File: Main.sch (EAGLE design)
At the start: 27 parts, among them IC2 74AHC1G125DBV, IC3 74AHC1G125DBV, M1 HX1, X1 BU-SMA-V

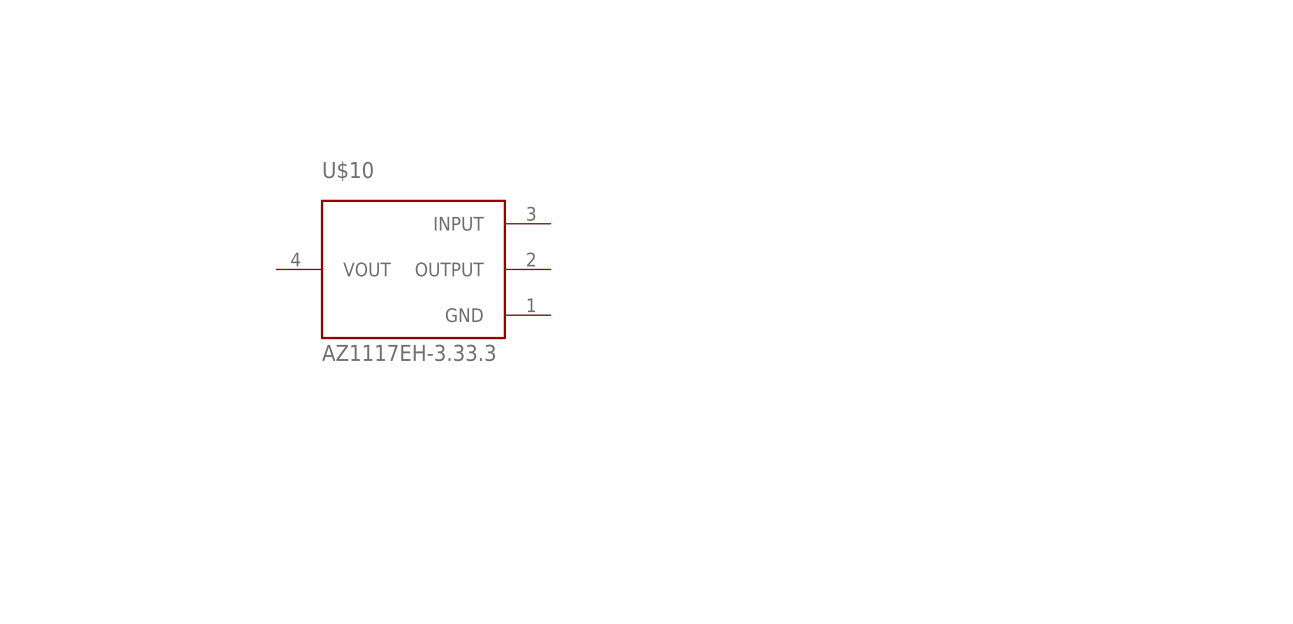
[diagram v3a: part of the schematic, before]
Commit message: Both Voltage Regs added and made
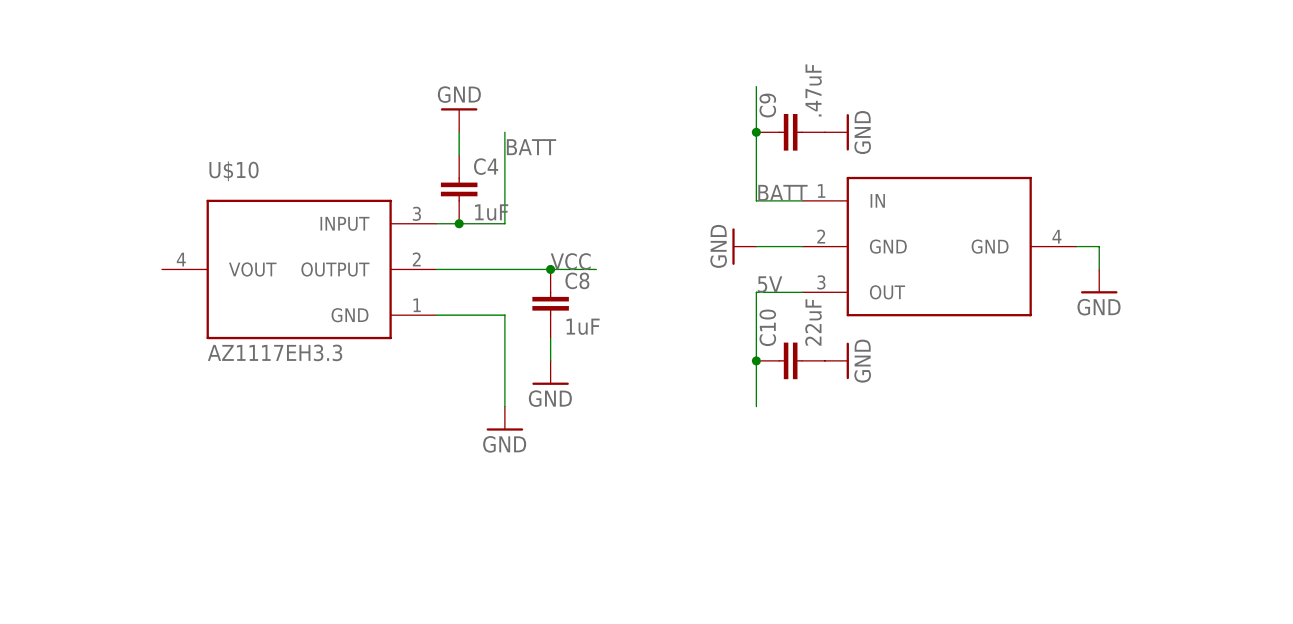
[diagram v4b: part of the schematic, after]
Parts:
- added C10: 22uF, SparkFun:CAP0603-CAP
- added C4, C8: 1uF, SparkFun:CAP0603-CAP
- added C9: .47uF, SparkFun:CAP0603-CAP
- added U$11: LM2940-5, Physoon:LM2940-5
- U$10: value AZ1117EH-3.33.3 -> AZ1117EH3.3; device Physoon:AZ1117EH-3.33.3 -> Physoon:AZ1117EH3.3
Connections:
- net 5V: now also C10.1, U$11.OUT
- net BATT: now also C4.2, C9.1, U$10.INPUT, U$11.IN
- net GND: now also C10.2, C4.1, C8.2, C9.2, U$10.GND, U$11.GND, U$11.GND@2
- net VCC: now also C8.1, U$10.OUTPUT
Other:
- moved on the sheet: U$10
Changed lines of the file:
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@@
 <setting verticaltext="up"/>
 </settings>
-<grid distance="0.1" unitdist="inch" unit="inch" style="lines" multiple="1" display="no" altdistance="0.01" altunitdist="inch" altunit="inch"/>
+<grid distance="0.1" unitdist="inch" unit="inch" style="lines" multiple="1" display="yes" altdistance="0.01" altunitdist="inch" altunit="inch"/>
 <layers>
 <layer number="1" name="Top" color="4" fill="1" visible="no" active="no"/>
@@
 <part name="GND23" library="SparkFun-Aesthetics" deviceset="GND" device=""/>
 <part name="GND24" library="SparkFun-Aesthetics" deviceset="GND" device=""/>
-<part name="U$10" library="Physoon" deviceset="AZ1117EH-3.3" device="3.3"/>
+<part name="U$10" library="Physoon" deviceset="AZ1117EH" device="3.3"/>
+<part name="GND25" library="SparkFun" deviceset="GND" device=""/>
+<part name="C4" library="SparkFun" deviceset="CAP" device="0603-CAP" value="1uF"/>
+<part name="C8" library="SparkFun" deviceset="CAP" device="0603-CAP" value="1uF"/>
+<part name="GND26" library="SparkFun" deviceset="GND" device=""/>
+<part name="GND27" library="SparkFun" deviceset="GND" device=""/>
+<part name="U$11" library="Physoon" deviceset="LM2940" device="-5"/>
+<part name="GND28" library="SparkFun" deviceset="GND" device=""/>
+<part name="GND29" library="SparkFun" deviceset="GND" device=""/>
+<part name="C9" library="SparkFun" deviceset="CAP" device="0603-CAP" value=".47uF"/>
+<part name="C10" library="SparkFun" deviceset="CAP" device="0603-CAP" value="22uF"/>
+<part name="GND30" library="SparkFun" deviceset="GND" device=""/>
+<part name="GND31" library="SparkFun" deviceset="GND" device=""/>
 </parts>
 <sheets>
@@
 <instance part="GND23" gate="1" x="2.54" y="66.04"/>
 <instance part="GND24" gate="1" x="-78.74" y="-29.21" rot="R270"/>
-<instance part="U$10" gate="G$1" x="71.12" y="185.42"/>
+<instance part="U$10" gate="G$1" x="58.42" y="185.42"/>
+<instance part="GND25" gate="1" x="81.28" y="167.64"/>
+<instance part="C4" gate="G$1" x="76.2" y="193.04"/>
+<instance part="C8" gate="G$1" x="86.36" y="180.34"/>
+<instance part="GND26" gate="1" x="86.36" y="172.72"/>
+<instance part="GND27" gate="1" x="76.2" y="203.2" rot="R180"/>
+<instance part="U$11" gate="G$1" x="129.54" y="187.96"/>
+<instance part="GND28" gate="1" x="106.68" y="187.96" rot="R270"/>
+<instance part="GND29" gate="1" x="147.32" y="182.88"/>
+<instance part="C9" gate="G$1" x="114.3" y="200.66" rot="R90"/>
+<instance part="C10" gate="G$1" x="114.3" y="175.26" rot="R90"/>
+<instance part="GND30" gate="1" x="119.38" y="200.66" rot="R90"/>
+<instance part="GND31" gate="1" x="119.38" y="175.26" rot="R90"/>
 </instances>
 <busses>
@@
 <junction x="109.22" y="45.72"/>
 <label x="109.22" y="43.18" size="1.778" layer="95"/>
+</segment>
+<segment>
+<pinref part="U$10" gate="G$1" pin="OUTPUT"/>
+<wire x1="73.66" y1="185.42" x2="86.36" y2="185.42" width="0.1524" layer="91"/>
+<label x="86.36" y="185.42" size="1.778" layer="95"/>
+<pinref part="C8" gate="G$1" pin="1"/>
+<wire x1="86.36" y1="185.42" x2="91.44" y2="185.42" width="0.1524" layer="91"/>
+<junction x="86.36" y="185.42"/>
 </segment>
 </net>
@@
 <wire x1="-71.12" y1="-29.21" x2="-76.2" y2="-29.21" width="0.1524" layer="91"/>
 <pinref part="GND24" gate="1" pin="GND"/>
+</segment>
+<segment>
+<pinref part="U$10" gate="G$1" pin="GND"/>
+<wire x1="73.66" y1="180.34" x2="81.28" y2="180.34" width="0.1524" layer="91"/>
+<wire x1="81.28" y1="180.34" x2="81.28" y2="170.18" width="0.1524" layer="91"/>
+<pinref part="GND25" gate="1" pin="GND"/>
+</segment>
+<segment>
+<pinref part="C8" gate="G$1" pin="2"/>
+<pinref part="GND26" gate="1" pin="GND"/>
+<wire x1="86.36" y1="175.26" x2="86.36" y2="177.8" width="0.1524" layer="91"/>
+</segment>
+<segment>
+<pinref part="C4" gate="G$1" pin="1"/>
+<pinref part="GND27" gate="1" pin="GND"/>
+<wire x1="76.2" y1="200.66" x2="76.2" y2="198.12" width="0.1524" layer="91"/>
+</segment>
+<segment>
+<pinref part="U$11" gate="G$1" pin="GND"/>
+<wire x1="114.3" y1="187.96" x2="109.22" y2="187.96" width="0.1524" layer="91"/>
+<pinref part="GND28" gate="1" pin="GND"/>
+</segment>
+<segment>
+<pinref part="U$11" gate="G$1" pin="GND@2"/>
+<wire x1="144.78" y1="187.96" x2="147.32" y2="187.96" width="0.1524" layer="91"/>
+<wire x1="147.32" y1="187.96" x2="147.32" y2="185.42" width="0.1524" layer="91"/>
+<pinref part="GND29" gate="1" pin="GND"/>
+</segment>
+<segment>
+<pinref part="C9" gate="G$1" pin="2"/>
+<pinref part="GND30" gate="1" pin="GND"/>
+</segment>
+<segment>
+<pinref part="C10" gate="G$1" pin="2"/>
+<pinref part="GND31" gate="1" pin="GND"/>
 </segment>
 </net>
@@
 <label x="-53.34" y="154.94" size="1.778" layer="95"/>
 </segment>
+<segment>
+<pinref part="U$11" gate="G$1" pin="OUT"/>
+<wire x1="114.3" y1="182.88" x2="109.22" y2="182.88" width="0.1524" layer="91"/>
+<wire x1="109.22" y1="182.88" x2="109.22" y2="175.26" width="0.1524" layer="91"/>
+<pinref part="C10" gate="G$1" pin="1"/>
+<wire x1="109.22" y1="175.26" x2="109.22" y2="170.18" width="0.1524" layer="91"/>
+<junction x="109.22" y="175.26"/>
+<label x="109.22" y="182.88" size="1.778" layer="95"/>
+</segment>
 </net>
 <net name="TXD-5V" class="0">
@@
 <label x="-41.91" y="-29.21" size="1.778" layer="95"/>
 </segment>
-</net>
+<segment>
+<pinref part="U$10" gate="G$1" pin="INPUT"/>
+<wire x1="73.66" y1="190.5" x2="76.2" y2="190.5" width="0.1524" layer="91"/>
+<wire x1="76.2" y1="190.5" x2="81.28" y2="190.5" width="0.1524" layer="91"/>
+<wire x1="81.28" y1="190.5" x2="81.28" y2="200.66" width="0.1524" layer="91"/>
+<label x="81.28" y="198.12" size="1.778" layer="95"/>
+<pinref part="C4" gate="G$1" pin="2"/>
+<junction x="76.2" y="190.5"/>
+</segment>
+<segment>
+<pinref part="U$11" gate="G$1" pin="IN"/>
+<wire x1="114.3" y1="193.04" x2="109.22" y2="193.04" width="0.1524" layer="91"/>
+<wire x1="109.22" y1="193.04" x2="109.22" y2="200.66" width="0.1524" layer="91"/>
+<pinref part="C9" gate="G$1" pin="1"/>
+<wire x1="109.22" y1="200.66" x2="109.22" y2="205.74" width="0.1524" layer="91"/>
+<junction x="109.22" y="200.66"/>
+<label x="109.22" y="193.04" size="1.778" layer="95"/>
+</segment>
+</net>

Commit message: More work
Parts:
- added JP4: (no value), SparkFun:M06POLAR
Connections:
- new net RXD: IC1.!!OC0CRXD0PD2, JP4.3
- new net SSC: IC1.PC4/OC1A/#SS, U$1.!CS!
- new net TXD: IC1.!!OC0DTXD0PD3, JP4.2
- net GND: now also JP4.5; no longer U$1.!CS!
- net VCC: now also IC1.AVCC, JP4.4
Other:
- moved on the sheet: C10
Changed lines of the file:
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@@
 <?xml version="1.0" encoding="utf-8"?>
 <!DOCTYPE eagle SYSTEM "eagle.dtd">
-<eagle version="8.1.0">
+<eagle version="6.5.0">
 <drawing>
 <settings>
@@
 <setting verticaltext="up"/>
 </settings>
-<grid distance="0.1" unitdist="inch" unit="inch" style="lines" multiple="1" display="yes" altdistance="0.01" altunitdist="inch" altunit="inch"/>
+<grid distance="0.1" unitdist="inch" unit="inch" style="lines" multiple="1" display="no" altdistance="0.01" altunitdist="inch" altunit="inch"/>
 <layers>
 <layer number="1" name="Top" color="4" fill="1" visible="no" active="no"/>
@@
 <part name="C7" library="SparkFun" deviceset="CAP" device="0805" value="100nF"/>
 <part name="GND12" library="SparkFun-Aesthetics" deviceset="GND" device=""/>
-<part name="GND13" library="SparkFun-Aesthetics" deviceset="GND" device=""/>
 <part name="GND14" library="SparkFun-Aesthetics" deviceset="GND" device=""/>
 <part name="X1" library="con-coax" deviceset="BU-SMA-V" device=""/>
@@
 <part name="GND30" library="SparkFun" deviceset="GND" device=""/>
 <part name="GND31" library="SparkFun" deviceset="GND" device=""/>
+<part name="JP4" library="SparkFun" deviceset="M06" device="POLAR"/>
 </parts>
 <sheets>
@@
 <instance part="C7" gate="G$1" x="-198.12" y="71.12"/>
 <instance part="GND12" gate="1" x="-198.12" y="63.5"/>
-<instance part="GND13" gate="1" x="-139.7" y="63.5"/>
 <instance part="GND14" gate="1" x="-38.1" y="195.58"/>
 <instance part="X1" gate="G$1" x="-50.8" y="200.66"/>
@@
 <instance part="GND29" gate="1" x="147.32" y="182.88"/>
 <instance part="C9" gate="G$1" x="114.3" y="200.66" rot="R90"/>
-<instance part="C10" gate="G$1" x="114.3" y="175.26" rot="R90"/>
+<instance part="C10" gate="G$1" x="114.3" y="172.72" rot="R90"/>
 <instance part="GND30" gate="1" x="119.38" y="200.66" rot="R90"/>
-<instance part="GND31" gate="1" x="119.38" y="175.26" rot="R90"/>
+<instance part="GND31" gate="1" x="119.38" y="172.72" rot="R90"/>
+<instance part="JP4" gate="G$1" x="55.88" y="144.78"/>
 </instances>
 <busses>
@@
 <wire x1="86.36" y1="185.42" x2="91.44" y2="185.42" width="0.1524" layer="91"/>
 <junction x="86.36" y="185.42"/>
+</segment>
+<segment>
+<pinref part="IC1" gate="G$1" pin="AVCC"/>
+<wire x1="109.22" y1="58.42" x2="116.84" y2="58.42" width="0.1524" layer="91"/>
+<label x="111.76" y="58.42" size="1.778" layer="95"/>
+</segment>
+<segment>
+<pinref part="JP4" gate="G$1" pin="4"/>
+<wire x1="60.96" y1="147.32" x2="71.12" y2="147.32" width="0.1524" layer="91"/>
+<label x="66.04" y="147.32" size="1.778" layer="95"/>
 </segment>
 </net>
@@
 </segment>
 <segment>
-<pinref part="U$1" gate="G$1" pin="!CS!"/>
-<wire x1="-152.4" y1="66.04" x2="-139.7" y2="66.04" width="0.1524" layer="91"/>
-<pinref part="GND13" gate="1" pin="GND"/>
-</segment>
-<segment>
 <pinref part="M1" gate="G$1" pin="RFGND1"/>
 <wire x1="-35.56" y1="203.2" x2="-38.1" y2="203.2" width="0.1524" layer="91"/>
@@
 <pinref part="C10" gate="G$1" pin="2"/>
 <pinref part="GND31" gate="1" pin="GND"/>
+</segment>
+<segment>
+<pinref part="JP4" gate="G$1" pin="5"/>
+<wire x1="60.96" y1="149.86" x2="71.12" y2="149.86" width="0.1524" layer="91"/>
+<label x="66.04" y="149.86" size="1.778" layer="95"/>
 </segment>
 </net>
@@
 <pinref part="U$11" gate="G$1" pin="OUT"/>
 <wire x1="114.3" y1="182.88" x2="109.22" y2="182.88" width="0.1524" layer="91"/>
-<wire x1="109.22" y1="182.88" x2="109.22" y2="175.26" width="0.1524" layer="91"/>
+<wire x1="109.22" y1="182.88" x2="109.22" y2="172.72" width="0.1524" layer="91"/>
 <pinref part="C10" gate="G$1" pin="1"/>
-<wire x1="109.22" y1="175.26" x2="109.22" y2="170.18" width="0.1524" layer="91"/>
-<junction x="109.22" y="175.26"/>
+<wire x1="109.22" y1="172.72" x2="109.22" y2="170.18" width="0.1524" layer="91"/>
+<junction x="109.22" y="172.72"/>
 <label x="109.22" y="182.88" size="1.778" layer="95"/>
 </segment>
@@
 </segment>
 </net>
+<net name="SSC" class="0">
+<segment>
+<pinref part="IC1" gate="G$1" pin="PC4/OC1A/#SS"/>
+<wire x1="48.26" y1="53.34" x2="38.1" y2="53.34" width="0.1524" layer="91"/>
+<label x="38.1" y="53.34" size="1.778" layer="95"/>
+</segment>
+<segment>
+<pinref part="U$1" gate="G$1" pin="!CS!"/>
+<wire x1="-152.4" y1="66.04" x2="-139.7" y2="66.04" width="0.1524" layer="91"/>
+<label x="-144.78" y="66.04" size="1.778" layer="95"/>
+</segment>
+</net>
+<net name="TXD" class="0">
+<segment>
+<pinref part="IC1" gate="G$1" pin="!!OC0DTXD0PD3"/>
+<wire x1="109.22" y1="93.98" x2="119.38" y2="93.98" width="0.1524" layer="91"/>
+<label x="114.3" y="93.98" size="1.778" layer="95"/>
+</segment>
+<segment>
+<pinref part="JP4" gate="G$1" pin="2"/>
+<wire x1="60.96" y1="142.24" x2="71.12" y2="142.24" width="0.1524" layer="91"/>
+<label x="66.04" y="142.24" size="1.778" layer="95"/>
+</segment>
+</net>
+<net name="RXD" class="0">
+<segment>
+<pinref part="IC1" gate="G$1" pin="!!OC0CRXD0PD2"/>
+<wire x1="109.22" y1="96.52" x2="119.38" y2="96.52" width="0.1524" layer="91"/>
+<label x="114.3" y="96.52" size="1.778" layer="95"/>
+</segment>
+<segment>
+<pinref part="JP4" gate="G$1" pin="3"/>
+<wire x1="60.96" y1="144.78" x2="71.12" y2="144.78" width="0.1524" layer="91"/>
+<label x="66.04" y="144.78" size="1.778" layer="95"/>
+</segment>
+</net>
